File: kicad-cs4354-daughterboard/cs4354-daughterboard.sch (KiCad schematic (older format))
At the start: 20 parts, among them J1 DAC1_pin1to7, J2 DAC2_pin1to7, J3 DAC1_pin8to14, J4 DAC2_pin8to14, J5 Conn_01x02_Male, J6 Conn_01x02_Male, J7 I2S3_MCK, J8 I2S3_WS, J9 +3.3V, U1 CS4354DAC

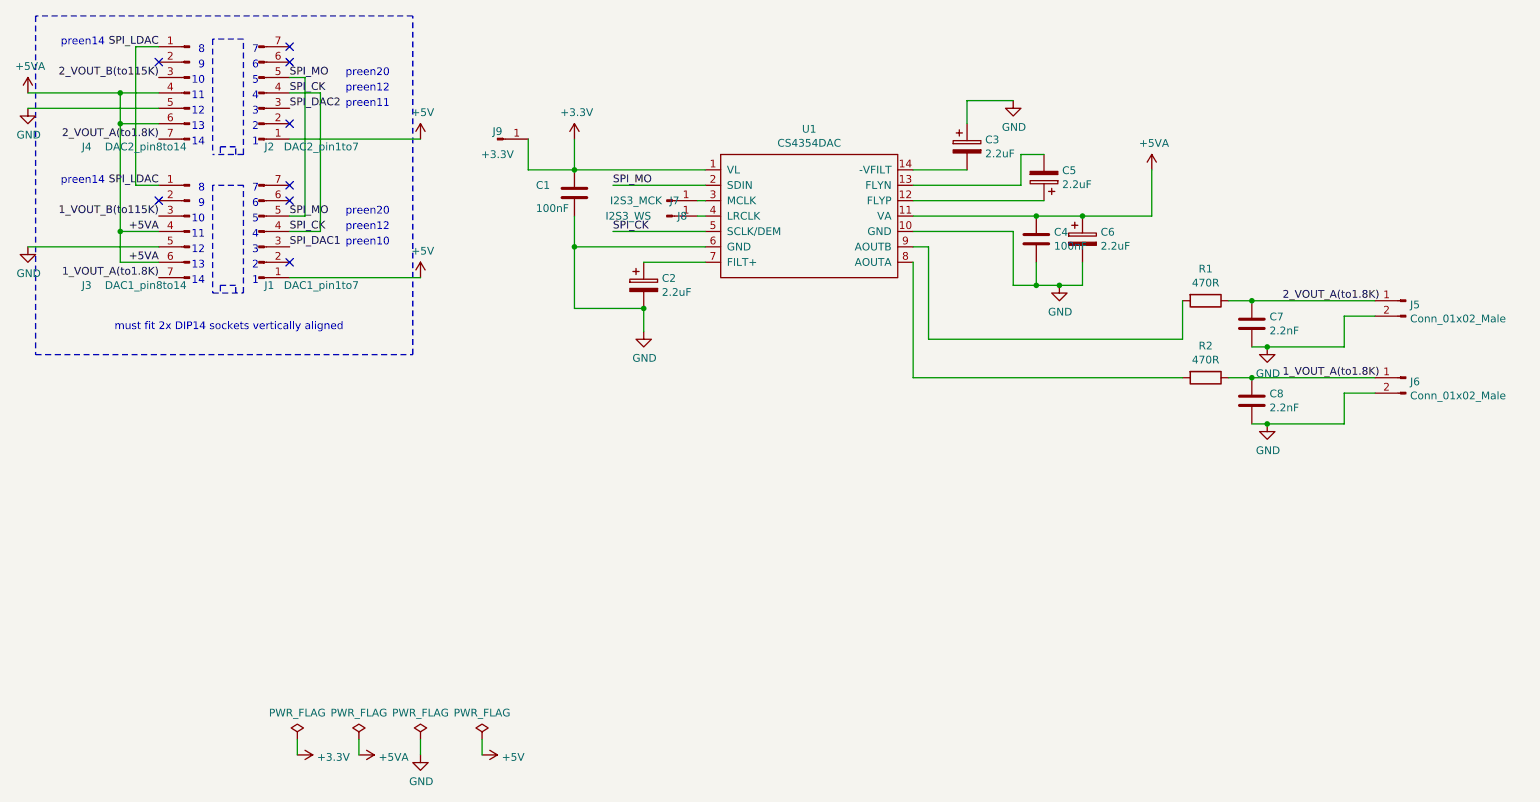
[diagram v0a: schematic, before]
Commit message: renamed kicad daughterboard 'noDIL'
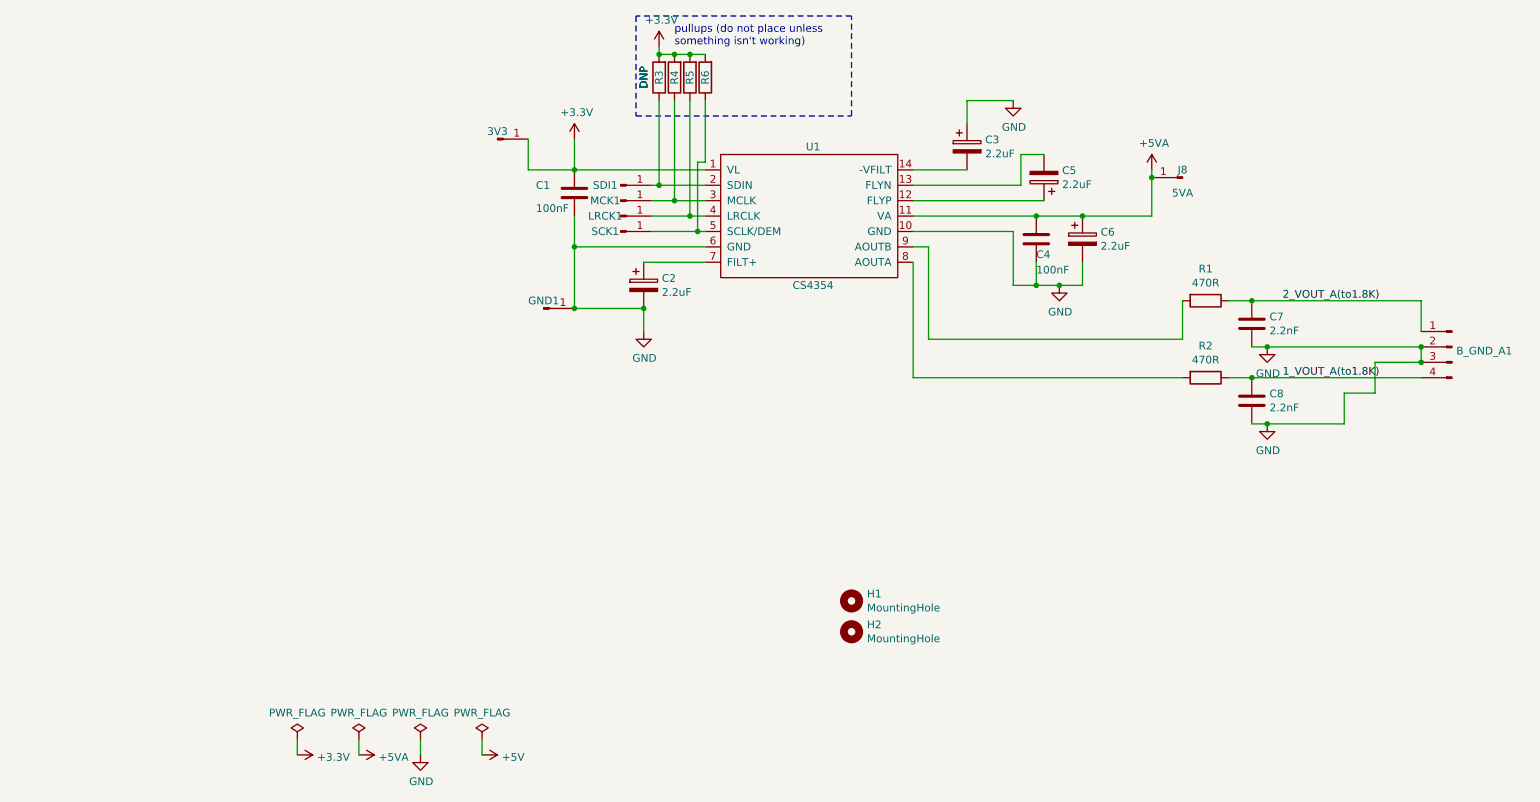
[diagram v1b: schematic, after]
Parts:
- removed J1: DAC1_pin1to7, Connector_PinHeader_2.54mm:PinHeader_1x07_P2.54mm_Vertical, symbol Connector:Conn_01x07_Male
- removed J2: DAC2_pin1to7, Connector_PinHeader_2.54mm:PinHeader_1x07_P2.54mm_Vertical, symbol Connector:Conn_01x07_Male
- removed J3: DAC1_pin8to14, Connector_PinHeader_2.54mm:PinHeader_1x07_P2.54mm_Vertical, symbol Connector:Conn_01x07_Male
- removed J4: DAC2_pin8to14, Connector_PinHeader_2.54mm:PinHeader_1x07_P2.54mm_Vertical, symbol Connector:Conn_01x07_Male
- removed J5, J6: Conn_01x02_Male, Connector_PinHeader_2.54mm:PinHeader_1x02_P2.54mm_Vertical, symbol Connector:Conn_01x02_Male
- added B_GND_A1: L GND R, Connector_PinHeader_2.54mm:PinHeader_1x04_P2.54mm_Vertical, symbol Connector:Conn_01x04_Male
- added GND1: GND, Connector_PinHeader_2.54mm:PinHeader_1x01_P2.54mm_Vertical, symbol Connector:Conn_01x01_Male
- added H1, H2: MountingHole, MountingHole:MountingHole_2.5mm, symbol Mechanical:MountingHole
- added J8: 5VA, Connector_PinHeader_2.54mm:PinHeader_1x01_P2.54mm_Vertical, symbol Connector:Conn_01x01_Male
- added R3, R4, R5, R6: DNP, Resistor_SMD:R_0805_2012Metric_Pad1.15x1.40mm_HandSolder, symbol Device:R
- added SCK1: SCK, Connector_PinHeader_2.54mm:PinHeader_1x01_P2.54mm_Vertical, symbol Connector:Conn_01x01_Male
- added SDI1: SDI, Connector_PinHeader_2.54mm:PinHeader_1x01_P2.54mm_Vertical, symbol Connector:Conn_01x01_Male
- 3V3: renamed from J9; value +3.3V -> 3V3
- LRCK1: renamed from J8; value I2S3_WS -> LRCK
- MCK1: renamed from J7; value I2S3_MCK -> MCK
- U1: value CS4354DAC -> CS4354
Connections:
- net +3V3: now also R3.2, R4.2, R5.2, R6.2
- net +5VA: now also J8.1 (Pin_1)
- net 1_VOUT_A(to1.8K): now also B_GND_A1.4 (Pin_4)
- net 2_VOUT_A(to1.8K): now also B_GND_A1.1 (Pin_1)
- net GND: now also B_GND_A1.2 (Pin_2), B_GND_A1.3 (Pin_3), GND1.1 (Pin_1)
- net at MCK1.1 (Pin_1), U1.3 (MCLK): now also R4.1
- net at LRCK1.1 (Pin_1), U1.4 (LRCLK): now also R5.1
- net SPI_CK: no longer names the net of U1.5 (SCLK/DEM)
- net SPI_CK: now also R6.1, SCK1.1 (Pin_1)
- net SPI_MO: no longer names the net of U1.2 (SDIN)
- net SPI_MO: now also R3.1, SDI1.1 (Pin_1)
- no-connect marks 8 -> 0
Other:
- note added: "pullups (do not place unless \nsomething isn't working)"
- note removed: "10"
- note removed: "11"
- note removed: "12"
- note removed: "13\n"
- note removed: "14"
- note removed: "1\n"
- note removed: "2"
- note removed: "3"
- note removed: "4"
- note removed: "5"
- note removed: "6"
- note removed: "7"
- note removed: "8"
- note removed: "9"
- note removed: "must fit 2x DIP14 sockets vertically aligned \n"
- note removed: "preen10"
- note removed: "preen11"
- note removed: "preen12"
- note removed: "preen14"
- note removed: "preen20"
- moved on the sheet: LRCK1, MCK1
